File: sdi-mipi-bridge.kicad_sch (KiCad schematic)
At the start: 186 parts, among them J1 Conn_BNC_031-70526-21, J2 Conn_BNC_031-70526-21, J3 Conn_FFC_68715014522_ONE-SIDE, J4 PinHeader_2x5_P1.27mm_Vertical, J5 PinHeader_1x4_P1.27mm_Drill.7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, J6 PinHeader_2x5_P1.27mm_Vertical, SW1 SW_SPST_KMR211NGLFS, U1 MAX8902B, U2 GS2971A, U3 GS2988, U4 CrossLink_LIF-MD6000-6JMG80I, U5 SC18IS602BIPW, Y1 Oscillator_SMD_27MHz_ABM7

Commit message: [#55723] Fix 2199SB-10G-301523
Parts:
- J4, J6: footprint sdi-mipi-bridge-footprints:PinHeader_2x05_P1.27mm_Vertical -> antmicro-footprints:PinHeader_2x5_P1.27mm_Drill0.65mm; symbol sdi-mipi-bridge:PinHeader_2x5_P1.27mm_Vertical -> antmicroGenericPinHeaders:PinHeader_2x5_P1.27mm_Drill0.65mm; Manufacturer Multicomp -> Multicomp Pro

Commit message: [#55723] Fix MC-HVT1-S04-G
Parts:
- J5: footprint sdi-mipi-bridge-footprints:PinHeader_1x4_P1.27mm_Drill.7mm -> antmicro-footprints:PinHeader_1x4_P1.27mm_Drill0.7mm; symbol sdi-mipi-bridge:PinHeader_1x4_P1.27mm_Drill.7mm -> antmicroGenericPinHeaders:PinHeader_1x4_P1.27mm_Drill0.7mm; Manufacturer Multicomp -> Multicomp Pro
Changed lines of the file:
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@@
     )
   )
-  (symbol (lib_id "sdi-mipi-bridge:PinHeader_1x4_P1.27mm_Drill.7mm") (at 35.56 154.94 0) (mirror y) (unit 1)
+  (symbol (lib_id "antmicroGenericPinHeaders:PinHeader_1x4_P1.27mm_Drill0.7mm") (at 35.56 154.94 0) (mirror y) (unit 1)
     (in_bom yes) (on_board yes) (dnp no) (fields_autoplaced)
     (property "Reference" "J5" (at 31.75 148.59 0)
@@
       (effects (font (size 1.27 1.27) (thickness 0.15)) (justify left bottom) hide)
     )
-    (property "Footprint" "sdi-mipi-bridge-footprints:PinHeader_1x4_P1.27mm_Drill.7mm" (at 15.24 167.64 0)
+    (property "Footprint" "antmicro-footprints:PinHeader_1x4_P1.27mm_Drill0.7mm" (at 15.24 167.64 0)
       (effects (font (size 1.27 1.27) (thickness 0.15)) (justify left bottom) hide)
     )
@@
       (effects (font (size 1.27 1.27) (thickness 0.15)))
     )
-    (property "Manufacturer" "Multicomp" (at 15.24 172.72 0)
+    (property "Manufacturer" "Multicomp Pro" (at 15.24 172.72 0)
       (effects (font (size 1.27 1.27) (thickness 0.15)) (justify left bottom) hide)
     )

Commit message: [#55723] Fix MAX8902B
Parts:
- U1: footprint sdi-mipi-bridge-footprints:TDFN-8-1EP_2x2mm_P0.5mm -> antmicro-footprints:TDFN-8-1EP_2x2mm_P0.5mm; symbol sdi-mipi-bridge:MAX8902B -> antmicroPMICVoltageRegulatorsLinear:MAX8902B; Manufacturer Maxim integrated -> Maxim Integrated Products
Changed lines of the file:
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@@
     )
   )
-  (symbol (lib_id "sdi-mipi-bridge:MAX8902B") (at 52.07 228.6 0) (unit 1)
+  (symbol (lib_id "antmicroPMICVoltageRegulatorsLinear:MAX8902B") (at 52.07 228.6 0) (unit 1)
     (in_bom yes) (on_board yes) (dnp no) (fields_autoplaced)
     (property "Reference" "U1" (at 59.69 222.25 0)
@@
       (effects (font (size 1.27 1.27) (thickness 0.15)) (justify left bottom) hide)
     )
-    (property "Footprint" "sdi-mipi-bridge-footprints:TDFN-8-1EP_2x2mm_P0.5mm" (at 86.36 227.33 0)
+    (property "Footprint" "antmicro-footprints:TDFN-8-1EP_2x2mm_P0.5mm" (at 80.01 241.3 0)
       (effects (font (size 1.27 1.27) (thickness 0.15)) (justify left bottom) hide)
     )
-    (property "Datasheet" "https://www.analog.com/media/en/technical-documentation/data-sheets/MAX8902-MAX8902B.pdf" (at 52.07 228.6 0)
+    (property "Datasheet" "https://www.analog.com/media/en/technical-documentation/data-sheets/MAX8902-MAX8902B.pdf" (at 80.01 243.84 0)
       (effects (font (size 1.27 1.27) (thickness 0.15)) (justify left bottom) hide)
     )
@@
       (effects (font (size 1.27 1.27) (thickness 0.15)))
     )
-    (property "Manufacturer" "Maxim integrated" (at 57.15 220.1164 0)
+    (property "Manufacturer" "Maxim Integrated Products" (at 80.01 246.38 0)
       (effects (font (size 1.27 1.27) (thickness 0.15)) (justify left bottom) hide)
     )

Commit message: [#55723] Fix LIF-MD6000-6JMG80I
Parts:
- U4: footprint sdi-mipi-bridge-footprints:BGA-80pin_ckfBGA80_7.0x7.0mm -> antmicro-footprints:BGA-80_7x7mm_Layout10x10_P0.65mm; symbol sdi-mipi-bridge:CrossLink_LIF-MD6000-6JMG80I -> antmicroFPGAChips:CrossLink_LIF-MD6000-6JMG80I; Manufacturer Lattice -> Lattice Semiconductor
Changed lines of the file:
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@@
     )
   )
-  (symbol (lib_id "sdi-mipi-bridge:CrossLink_LIF-MD6000-6JMG80I") (at 459.74 241.3 0) (unit 1)
+  (symbol (lib_id "antmicroFPGAChips:CrossLink_LIF-MD6000-6JMG80I") (at 459.74 241.3 0) (unit 1)
     (in_bom yes) (on_board yes) (dnp no) (fields_autoplaced)
     (property "Reference" "U4" (at 491.49 233.68 0)
@@
       (effects (font (size 1.27 1.27) (thickness 0.15)) (justify left bottom) hide)
     )
-    (property "Footprint" "sdi-mipi-bridge-footprints:BGA-80pin_ckfBGA80_7.0x7.0mm" (at 463.55 230.505 0)
+    (property "Footprint" "antmicro-footprints:BGA-80_7x7mm_Layout10x10_P0.65mm" (at 538.48 255.27 0)
       (effects (font (size 1.27 1.27) (thickness 0.15)) (justify left bottom) hide)
     )
-    (property "Datasheet" "https://www.latticesemi.com/view_document?document_id=51662" (at 463.55 235.585 0)
+    (property "Datasheet" "https://www.latticesemi.com/view_document?document_id=51662" (at 538.48 257.81 0)
       (effects (font (size 1.27 1.27) (thickness 0.15)) (justify left bottom) hide)
     )
@@
       (effects (font (size 1.27 1.27) (thickness 0.15)))
     )
-    (property "Manufacturer" "Lattice" (at 459.74 241.3 0)
+    (property "Manufacturer" "Lattice Semiconductor" (at 538.48 260.35 0)
       (effects (font (size 1.27 1.27) (thickness 0.15)) (justify left bottom) hide)
     )

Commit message: [#55723] Run loclib
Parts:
- J4, J6: footprint antmicro-footprints:PinHeader_2x5_P1.27mm_Drill0.65mm -> sdi-mipi-bridge-footprints:PinHeader_2x5_P1.27mm_Drill0.65mm; symbol antmicroGenericPinHeaders:PinHeader_2x5_P1.27mm_Drill0.65mm -> sdi-mipi-bridge:PinHeader_2x5_P1.27mm_Drill0.65mm
- J5: footprint antmicro-footprints:PinHeader_1x4_P1.27mm_Drill0.7mm -> sdi-mipi-bridge-footprints:PinHeader_1x4_P1.27mm_Drill0.7mm; symbol antmicroGenericPinHeaders:PinHeader_1x4_P1.27mm_Drill0.7mm -> sdi-mipi-bridge:PinHeader_1x4_P1.27mm_Drill0.7mm
- U1: footprint antmicro-footprints:TDFN-8-1EP_2x2mm_P0.5mm -> sdi-mipi-bridge-footprints:TDFN-8-1EP_2x2mm_P0.5mm; symbol antmicroPMICVoltageRegulatorsLinear:MAX8902B -> sdi-mipi-bridge:MAX8902B
- U4: footprint antmicro-footprints:BGA-80_7x7mm_Layout10x10_P0.65mm -> sdi-mipi-bridge-footprints:BGA-80_7x7mm_Layout10x10_P0.65mm; symbol antmicroFPGAChips:CrossLink_LIF-MD6000-6JMG80I -> sdi-mipi-bridge:CrossLink_LIF-MD6000-6JMG80I
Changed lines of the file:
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@@
     )
   )
-  (symbol (lib_id "antmicroPMICVoltageRegulatorsLinear:MAX8902B") (at 52.07 228.6 0) (unit 1)
+  (symbol (lib_id "sdi-mipi-bridge:MAX8902B") (at 52.07 228.6 0) (unit 1)
     (in_bom yes) (on_board yes) (dnp no) (fields_autoplaced)
     (property "Reference" "U1" (at 59.69 222.25 0)
@@
       (effects (font (size 1.27 1.27) (thickness 0.15)) (justify left bottom) hide)
     )
-    (property "Footprint" "antmicro-footprints:TDFN-8-1EP_2x2mm_P0.5mm" (at 80.01 241.3 0)
+    (property "Footprint" "sdi-mipi-bridge-footprints:TDFN-8-1EP_2x2mm_P0.5mm" (at 80.01 241.3 0)
       (effects (font (size 1.27 1.27) (thickness 0.15)) (justify left bottom) hide)
     )
@@
     )
   )
-  (symbol (lib_id "antmicroFPGAChips:CrossLink_LIF-MD6000-6JMG80I") (at 459.74 241.3 0) (unit 1)
+  (symbol (lib_id "sdi-mipi-bridge:CrossLink_LIF-MD6000-6JMG80I") (at 459.74 241.3 0) (unit 1)
     (in_bom yes) (on_board yes) (dnp no) (fields_autoplaced)
     (property "Reference" "U4" (at 491.49 233.68 0)
@@
       (effects (font (size 1.27 1.27) (thickness 0.15)) (justify left bottom) hide)
     )
-    (property "Footprint" "antmicro-footprints:BGA-80_7x7mm_Layout10x10_P0.65mm" (at 538.48 255.27 0)
+    (property "Footprint" "sdi-mipi-bridge-footprints:BGA-80_7x7mm_Layout10x10_P0.65mm" (at 538.48 255.27 0)
       (effects (font (size 1.27 1.27) (thickness 0.15)) (justify left bottom) hide)
     )
@@
     )
   )
-  (symbol (lib_id "antmicroGenericPinHeaders:PinHeader_1x4_P1.27mm_Drill0.7mm") (at 35.56 154.94 0) (mirror y) (unit 1)
+  (symbol (lib_id "sdi-mipi-bridge:PinHeader_1x4_P1.27mm_Drill0.7mm") (at 35.56 154.94 0) (mirror y) (unit 1)
     (in_bom yes) (on_board yes) (dnp no) (fields_autoplaced)
     (property "Reference" "J5" (at 31.75 148.59 0)
@@
       (effects (font (size 1.27 1.27) (thickness 0.15)) (justify left bottom) hide)
     )
-    (property "Footprint" "antmicro-footprints:PinHeader_1x4_P1.27mm_Drill0.7mm" (at 15.24 167.64 0)
+    (property "Footprint" "sdi-mipi-bridge-footprints:PinHeader_1x4_P1.27mm_Drill0.7mm" (at 15.24 167.64 0)
       (effects (font (size 1.27 1.27) (thickness 0.15)) (justify left bottom) hide)
     )
@@
     )
   )
-  (symbol (lib_id "antmicroGenericPinHeaders:PinHeader_2x5_P1.27mm_Drill0.65mm") (at 34.29 119.38 0) (unit 1)
+  (symbol (lib_id "sdi-mipi-bridge:PinHeader_2x5_P1.27mm_Drill0.65mm") (at 34.29 119.38 0) (unit 1)
     (in_bom yes) (on_board yes) (dnp no) (fields_autoplaced)
     (property "Reference" "J6" (at 39.37 113.03 0)
@@
       (effects (font (size 1.27 1.27) (thickness 0.15)) (justify left bottom) hide)
     )
-    (property "Footprint" "antmicro-footprints:PinHeader_2x5_P1.27mm_Drill0.65mm" (at 59.69 132.08 0)
+    (property "Footprint" "sdi-mipi-bridge-footprints:PinHeader_2x5_P1.27mm_Drill0.65mm" (at 59.69 132.08 0)
       (effects (font (size 1.27 1.27) (thickness 0.15)) (justify left bottom) hide)
     )
@@
     )
   )
-  (symbol (lib_id "antmicroGenericPinHeaders:PinHeader_2x5_P1.27mm_Drill0.65mm") (at 532.13 100.33 0) (unit 1)
+  (symbol (lib_id "sdi-mipi-bridge:PinHeader_2x5_P1.27mm_Drill0.65mm") (at 532.13 100.33 0) (unit 1)
     (in_bom yes) (on_board yes) (dnp no) (fields_autoplaced)
     (property "Reference" "J4" (at 537.21 93.98 0)
@@
       (effects (font (size 1.27 1.27) (thickness 0.15)) (justify left bottom) hide)
     )
-    (property "Footprint" "antmicro-footprints:PinHeader_2x5_P1.27mm_Drill0.65mm" (at 557.53 113.03 0)
+    (property "Footprint" "sdi-mipi-bridge-footprints:PinHeader_2x5_P1.27mm_Drill0.65mm" (at 557.53 113.03 0)
       (effects (font (size 1.27 1.27) (thickness 0.15)) (justify left bottom) hide)
     )

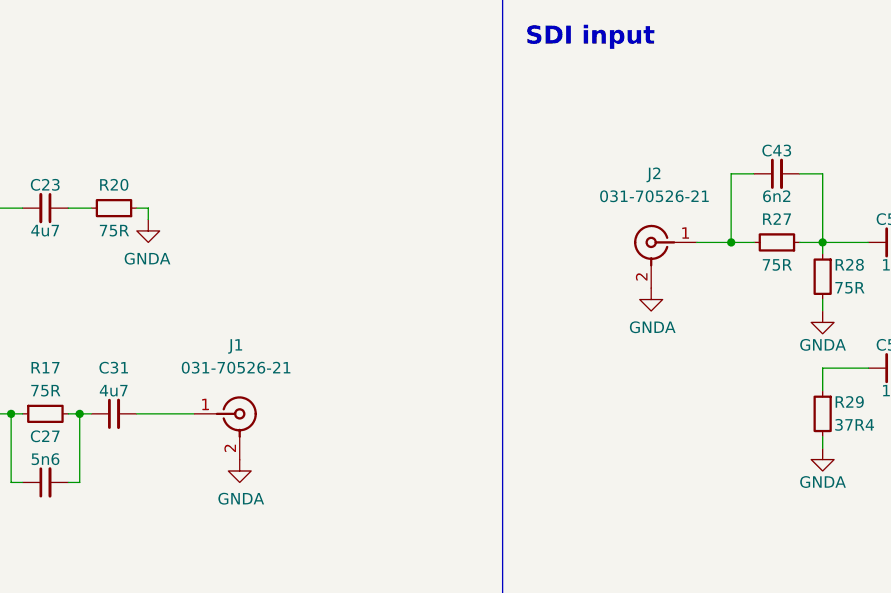
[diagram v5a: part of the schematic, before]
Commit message: [#55723] Fix Conn_BNC_031-70526-21
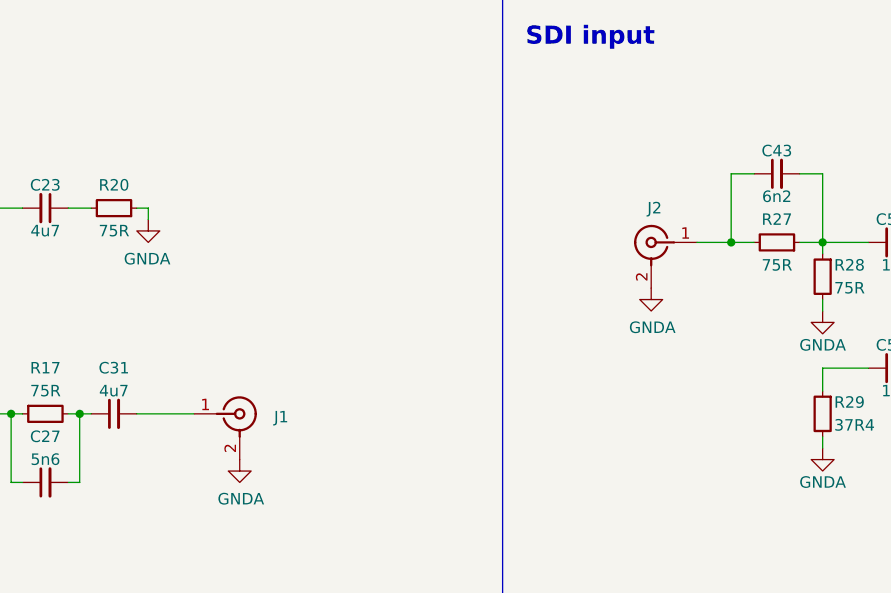
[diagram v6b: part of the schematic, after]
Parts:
- J1, J2: footprint sdi-mipi-bridge-footprints:Conn_BNC_031-70526-21 -> antmicro-footprints:Conn_BNC_031-70526-21; symbol sdi-mipi-bridge:Conn_BNC_031-70526-21 -> antmicroCoaxialConnectorsRF:Conn_BNC_031-70526-21
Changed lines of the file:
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@@
     )
   )
-  (symbol (lib_id "sdi-mipi-bridge:Conn_BNC_031-70526-21") (at 245.11 140.97 0) (mirror y) (unit 1)
+  (symbol (lib_id "antmicroCoaxialConnectorsRF:Conn_BNC_031-70526-21") (at 245.11 140.97 0) (mirror y) (unit 1)
     (in_bom yes) (on_board yes) (dnp no) (fields_autoplaced)
-    (property "Reference" "J2" (at 240.4109 133.35 0)
+    (property "Reference" "J2" (at 240.4109 137.16 0)
       (effects (font (size 1.27 1.27)))
     )
@@
       (effects (font (size 1.27 1.27) (thickness 0.15)) (justify left bottom) hide)
     )
-    (property "Footprint" "sdi-mipi-bridge-footprints:Conn_BNC_031-70526-21" (at 224.79 151.13 0)
+    (property "Footprint" "antmicro-footprints:Conn_BNC_031-70526-21" (at 224.79 151.13 0)
       (effects (font (size 1.27 1.27) (thickness 0.15)) (justify left bottom) hide)
     )
@@
       (effects (font (size 1.27 1.27) (thickness 0.15)) (justify left bottom) hide)
     )
-    (property "MPN" "031-70526-21" (at 240.4109 135.89 0)
-      (effects (font (size 1.27 1.27) (thickness 0.15)))
+    (property "MPN" "031-70526-21" (at 224.79 156.21 0)
+      (effects (font (size 1.27 1.27) (thickness 0.15)) (justify left bottom) hide)
     )
     (property "Manufacturer" "Amphenol" (at 224.79 158.75 0)
@@
     )
   )
-  (symbol (lib_id "sdi-mipi-bridge:Conn_BNC_031-70526-21") (at 189.23 160.02 0) (unit 1)
+  (symbol (lib_id "antmicroCoaxialConnectorsRF:Conn_BNC_031-70526-21") (at 189.23 160.02 0) (unit 1)
     (in_bom yes) (on_board yes) (dnp no) (fields_autoplaced)
-    (property "Reference" "J1" (at 193.929 152.4 0)
-      (effects (font (size 1.27 1.27)))
+    (property "Reference" "J1" (at 198.12 160.3767 0)
+      (effects (font (size 1.27 1.27)) (justify left))
     )
     (property "Value" "Conn_BNC_031-70526-21" (at 198.12 161.6466 0)
       (effects (font (size 1.27 1.27) (thickness 0.15)) (justify left) hide)
     )
-    (property "Footprint" "sdi-mipi-bridge-footprints:Conn_BNC_031-70526-21" (at 209.55 170.18 0)
+    (property "Footprint" "antmicro-footprints:Conn_BNC_031-70526-21" (at 209.55 170.18 0)
       (effects (font (size 1.27 1.27) (thickness 0.15)) (justify left bottom) hide)
     )
@@
       (effects (font (size 1.27 1.27) (thickness 0.15)) (justify left bottom) hide)
     )
-    (property "MPN" "031-70526-21" (at 193.929 154.94 0)
-      (effects (font (size 1.27 1.27) (thickness 0.15)))
+    (property "MPN" "031-70526-21" (at 209.55 175.26 0)
+      (effects (font (size 1.27 1.27) (thickness 0.15)) (justify left bottom) hide)
     )
     (property "Manufacturer" "Amphenol" (at 209.55 177.8 0)

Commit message: [#55723] Run loclib
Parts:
- J1, J2: footprint antmicro-footprints:Conn_BNC_031-70526-21 -> sdi-mipi-bridge-footprints:Conn_BNC_031-70526-21; symbol antmicroCoaxialConnectorsRF:Conn_BNC_031-70526-21 -> sdi-mipi-bridge:Conn_BNC_031-70526-21
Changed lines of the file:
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@@
     )
   )
-  (symbol (lib_id "antmicroCoaxialConnectorsRF:Conn_BNC_031-70526-21") (at 245.11 140.97 0) (mirror y) (unit 1)
+  (symbol (lib_id "sdi-mipi-bridge:Conn_BNC_031-70526-21") (at 245.11 140.97 0) (mirror y) (unit 1)
     (in_bom yes) (on_board yes) (dnp no) (fields_autoplaced)
     (property "Reference" "J2" (at 240.4109 137.16 0)
@@
       (effects (font (size 1.27 1.27) (thickness 0.15)) (justify left bottom) hide)
     )
-    (property "Footprint" "antmicro-footprints:Conn_BNC_031-70526-21" (at 224.79 151.13 0)
+    (property "Footprint" "sdi-mipi-bridge-footprints:Conn_BNC_031-70526-21" (at 224.79 151.13 0)
       (effects (font (size 1.27 1.27) (thickness 0.15)) (justify left bottom) hide)
     )
@@
     )
   )
-  (symbol (lib_id "antmicroCoaxialConnectorsRF:Conn_BNC_031-70526-21") (at 189.23 160.02 0) (unit 1)
+  (symbol (lib_id "sdi-mipi-bridge:Conn_BNC_031-70526-21") (at 189.23 160.02 0) (unit 1)
     (in_bom yes) (on_board yes) (dnp no) (fields_autoplaced)
     (property "Reference" "J1" (at 198.12 160.3767 0)
@@
       (effects (font (size 1.27 1.27) (thickness 0.15)) (justify left) hide)
     )
-    (property "Footprint" "antmicro-footprints:Conn_BNC_031-70526-21" (at 209.55 170.18 0)
-      (effects (font (size 1.27 1.27) (thickness 0.15)) (justify left bottom) hide)
-    )
+    (property "Footprint" "sdi-mipi-bridge-footprints:Conn_BNC_031-70526-21" (at 209.55 170.18 0)
+      (effects (font (size 1.27 1.27) (thickness 0.15)) (justify left bottom) hide)
+    )
